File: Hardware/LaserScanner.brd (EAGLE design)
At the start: 160 x 100 mm, 35 parts, among them J1 USB, Q1 MBT3904DW1T1, U1 ESP-WROOM-32, U2 3.3V, U3 CH340C

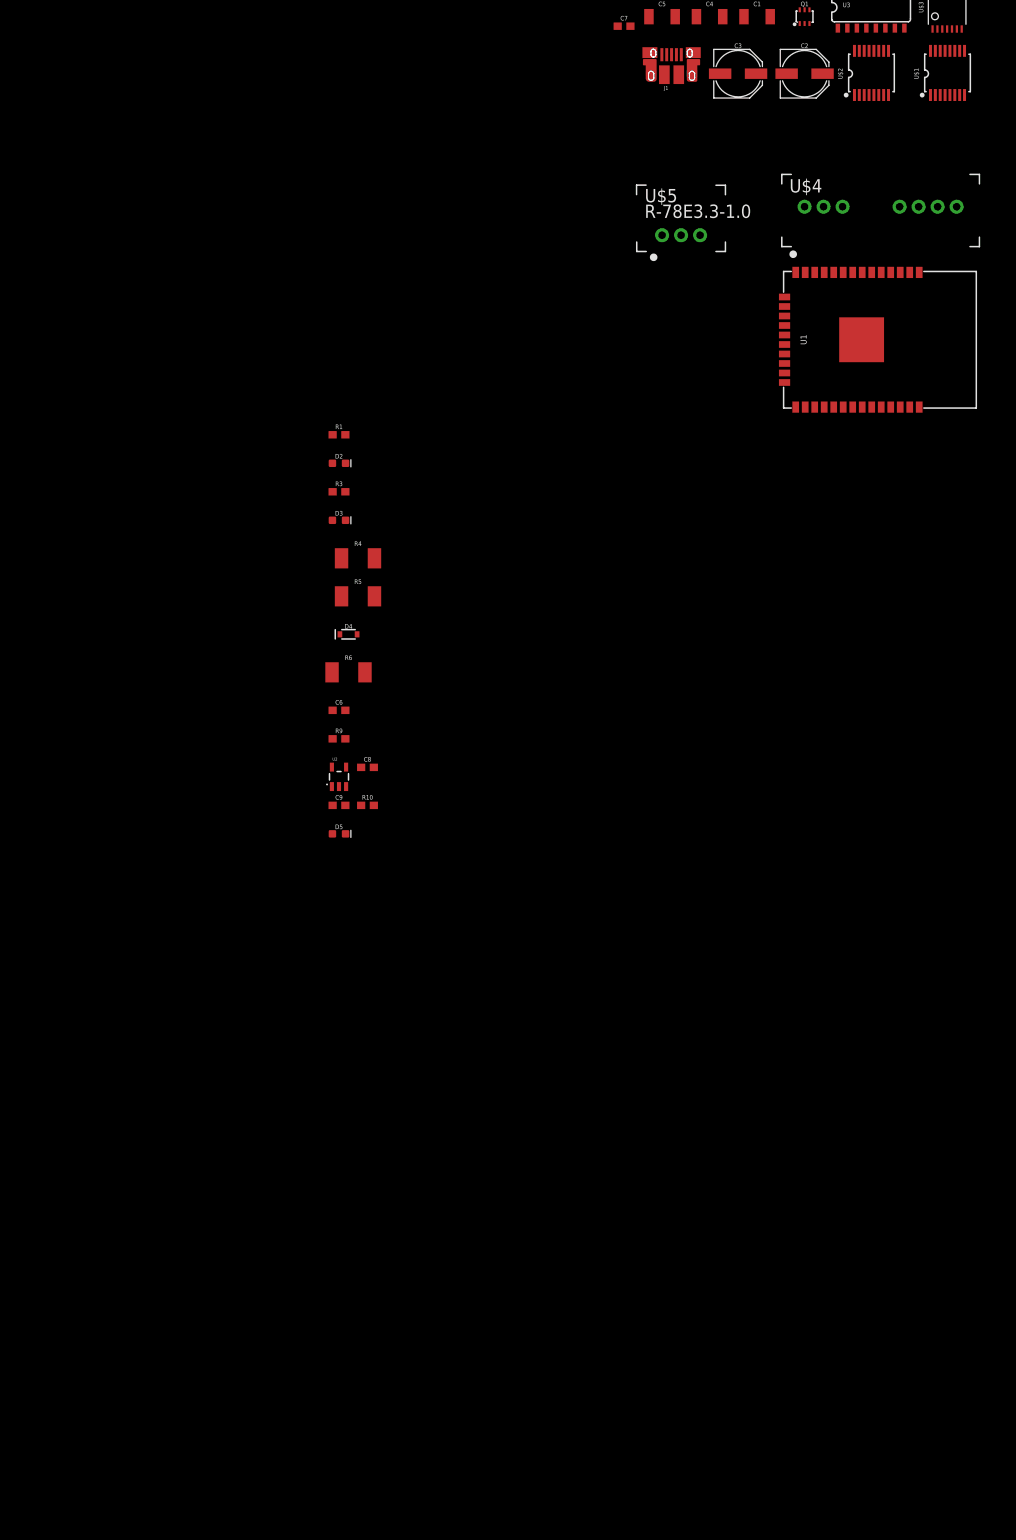
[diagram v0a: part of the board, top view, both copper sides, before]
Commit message: Added DAC circuits and power interlocks
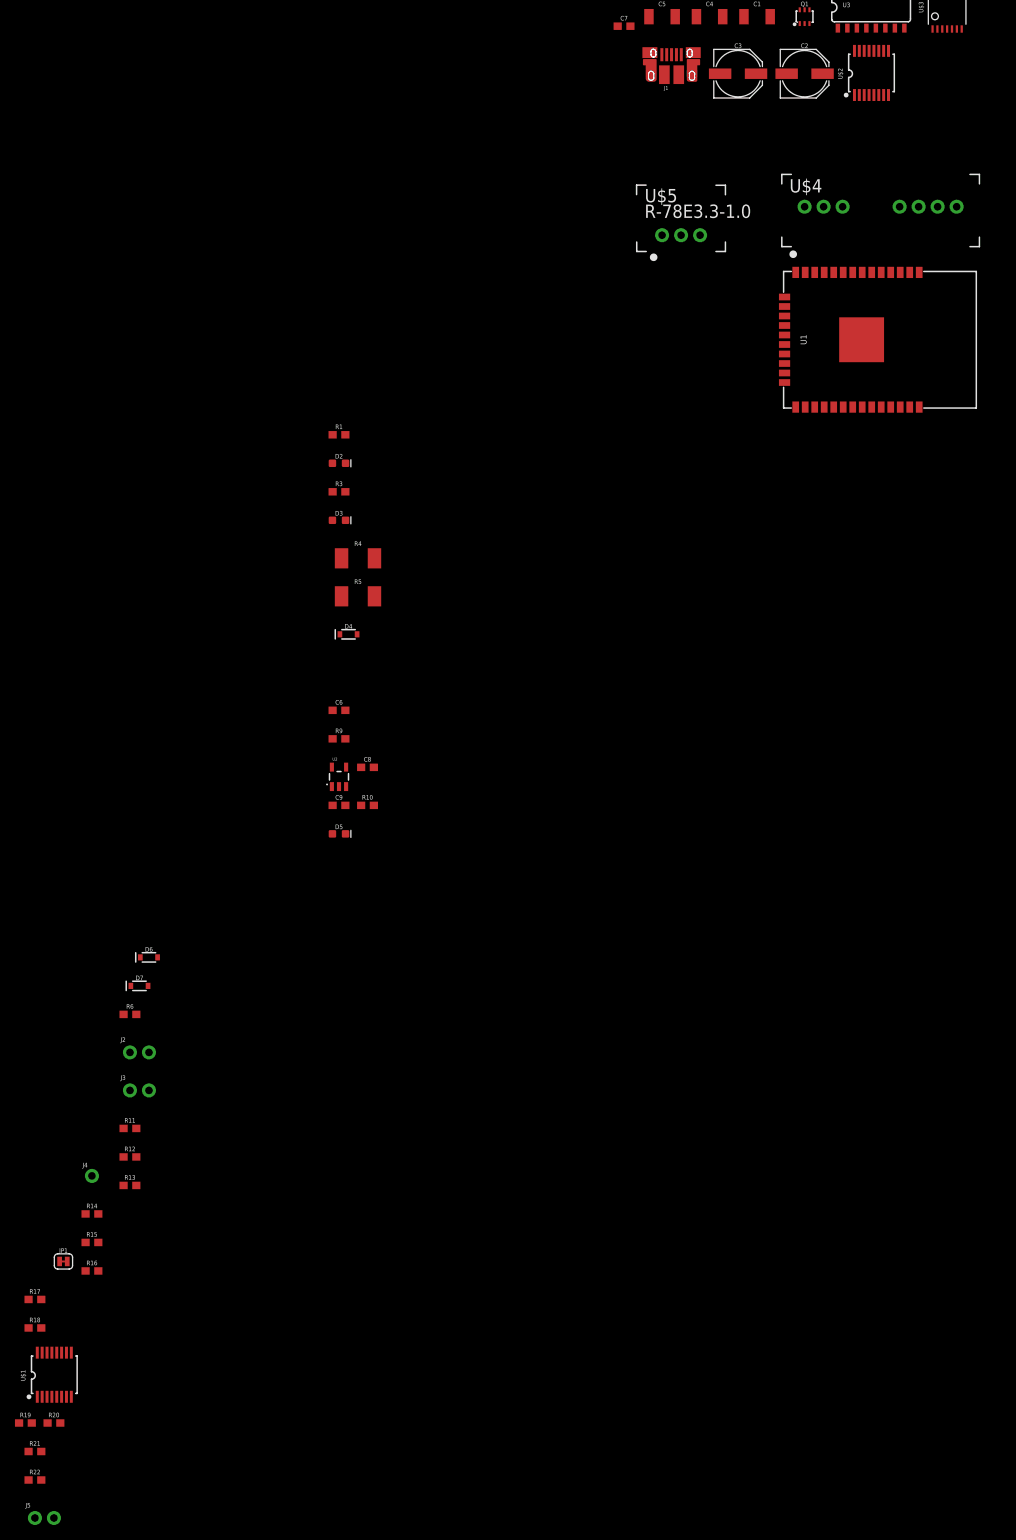
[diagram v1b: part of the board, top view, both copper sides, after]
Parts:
- added D6, D7: 3A/10V/280mV, SparkFun-DiscreteSemi:SOD-323
- added J2: SHTDWN, SparkFun-Connectors:1X02_NO_SILK
- added J3: KEYSWITCH, SparkFun-Connectors:1X02_NO_SILK
- added J4: (no value), SparkFun-Connectors:1X01_NO_SILK
- added J5: ESTOP, SparkFun-Connectors:1X02_NO_SILK
- added JP1: JUMPER-SMT_2_NC_TRACE_SILK, SparkFun-Jumpers:SMT-JUMPER_2_NC_TRACE_SILK
- added R11, R12, R13, R14, R15, R16, R17, R18, R19, R20, R21, R22: 10k, SparkFun-Resistors:0603
- R6: value 510 -> 3.3k; device SparkFun-Resistors:2010 -> SparkFun-Resistors:0603
- moved U$1 211.0 mm to (-137.2, -128.3)
- moved R6 54.3 mm to (-127.0, -80.0)
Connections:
- new net AGND: JP1.1, U$1.4, U$2.4
- new net AUX_OUT: J4.1, R14.2, U$3.10
- new net GX_!CS: R17.1, U$2.12
- new net GX_!LDAC: R18.1, U$2.15
- new net GX_!RST: U$2.11
- new net GX_OUT: U$2.1
- new net GY_!CS: R19.1, U$1.12
- new net GY_!LDAC: R20.1, U$1.15
- new net GY_!RST: U$1.11
- new net GY_OUT: U$1.1
- new net G_MOSI: U$1.14, U$2.14
- new net G_SCLK: U$1.13, U$2.13
- new net LASER_B: R13.2, U$3.5
- new net LASER_G: R12.2, U$3.11
- new net LASER_R: R11.2, U$3.4
- new net L_!CLR: R15.1, U$3.9
- new net L_!LDAC: R21.1, U$3.1
- new net L_!SYNC: R22.1, U$3.2
- new net L_MOSI: U$3.13
- new net L_SCLK: U$3.14
- new net N$7: C4.1, D6.A, U$5.3
- new net N$9: J3.2, J5.1
- new net VCC: J2.1, J5.2
- new net VCC_SWITCHED: C5.1, J3.1, U$4.2
- new net VREFH: U$1.5, U$1.6, U$2.5, U$2.6
- new net VREFL: U$1.7, U$1.8, U$2.7, U$2.8
- net -12V: now also U$1.3, U$2.3
- net 12V: now also U$1.2, U$2.2
- net 3.3V: now also R15.2, R17.2, R18.2, R19.2, R20.2, R21.2, R22.2, U$1.10, U$1.9, U$2.10, U$2.9
- net 5V: now also C8.1, D6.C, D7.C, U$3.3, U$3.7, U2.1, U2.3; no longer C4.1, U$5.3
- net GND: now also JP1.2, R11.1, R12.1, R13.1, R14.1, R16.1, U$1.16, U$2.16, U$3.12, U$3.6
- net N$2: now also R16.2, U$3.8; no longer C5.1, U$4.2
- net N$4: now also R6.2; no longer R6.1
- net SHTDWN: now also J2.2, R6.1; no longer R6.2
- net V_USB: now also D7.A; no longer C8.1, U2.1, U2.3

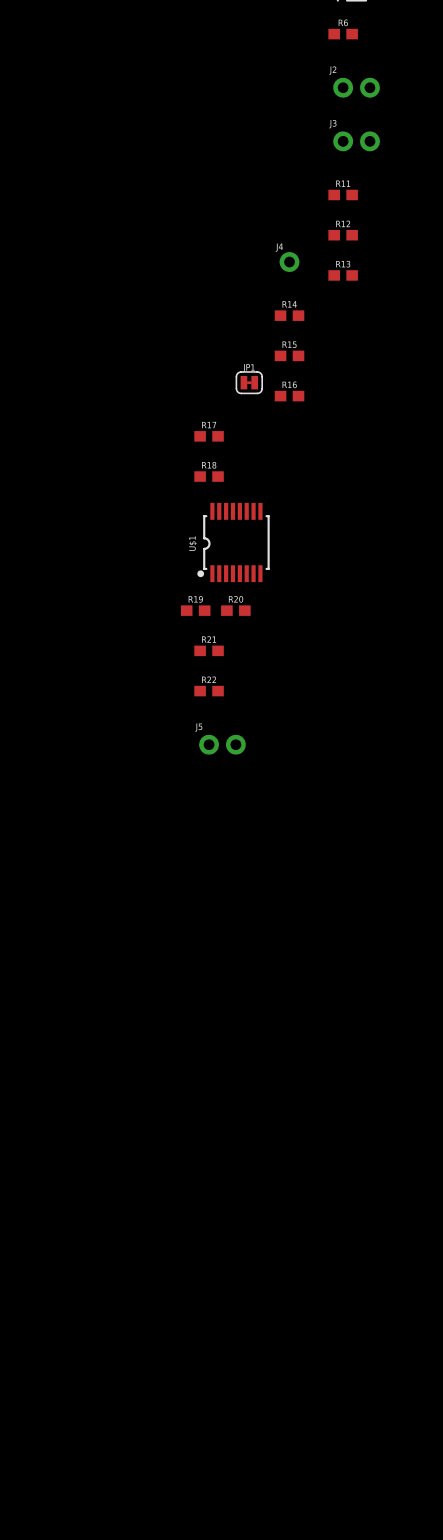
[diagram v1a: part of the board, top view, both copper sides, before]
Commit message: Add KILL signal and VREF delay
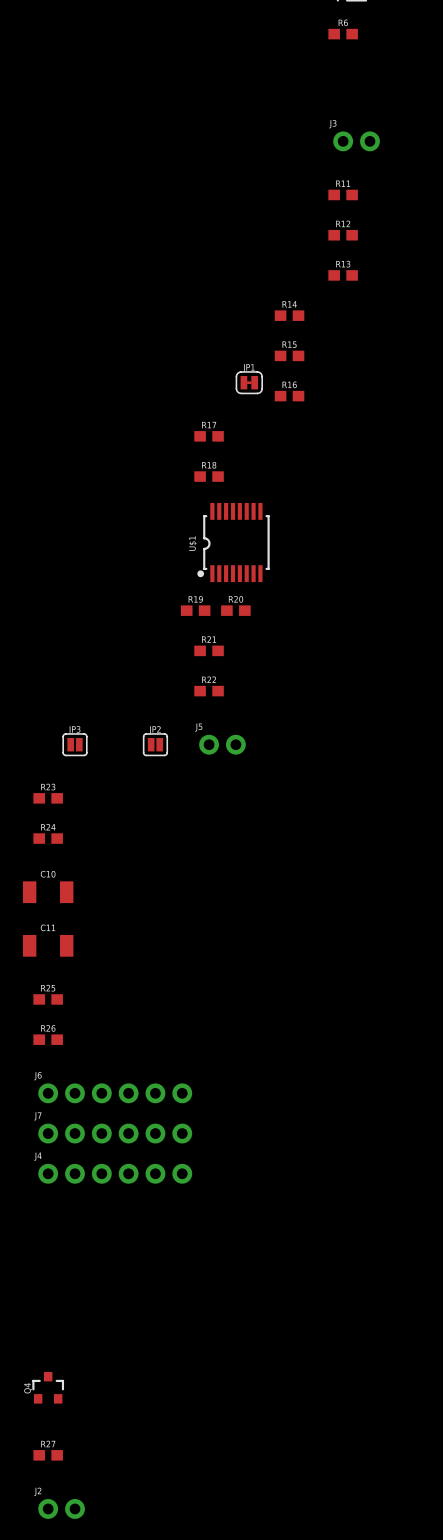
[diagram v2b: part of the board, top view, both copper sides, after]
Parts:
- added C10, C11: 10uF, SparkFun-Capacitors:1210
- added J6, J7: (no value), SparkFun-Connectors:1X06_NO_SILK
- added JP2, JP3: JUMPER-SMT_2_NO_SILK, SparkFun-Jumpers:SMT-JUMPER_2_NO_SILK
- added Q4: 2.5A/30V/105mΩ, SparkFun-DiscreteSemi:SOT23-3
- added R23, R24, R25, R26, R27: 10k, SparkFun-Resistors:0603
- J2: value SHTDWN -> !KILL!
- J4: device SparkFun-Connectors:1X01_NO_SILK -> SparkFun-Connectors:1X06_NO_SILK
- moved J2 137.5 mm to (-154.9, -219.7)
- moved J4 89.3 mm to (-154.9, -188.0)
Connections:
- removed net MISO: U1.14
- removed net MOSI: U1.16
- removed net SCLK: U1.13
- new net !KILL: J2.2, Q4.1, R27.2
- new net N$11: U1.29
- new net N$22: U1.8
- new net N$23: U1.9
- new net N$24: U1.6
- new net N$25: U1.7
- new net N$8: U1.26
- net -12V: now also JP3.1, R23.1
- net 12V: now also JP2.1, R24.1
- net 3.3V: now also R25.2, R26.2
- net AGND: now also C10.2, C11.2, J7.1, J7.2, J7.3, J7.4, J7.5, J7.6
- net AUX_OUT: now also J6.6; no longer J4.1
- net GND: now also J4.1, J4.2, J4.3, J4.4, J4.5, J4.6, R27.1
- net GX_!CS: now also U1.33
- net GX_!LDAC: now also U1.31
- net GX_!RST: now also R25.1, U1.36
- net GX_OUT: now also J6.1
- net GY_!CS: now also U1.27
- net GY_!LDAC: now also U1.23
- net GY_!RST: now also R26.1, U1.28
- net GY_OUT: now also J6.2
- net G_MOSI: now also U1.16
- net G_SCLK: now also U1.13
- net LASER_B: now also J6.5
- net LASER_G: now also J6.4
- net LASER_R: now also J6.3
- net L_!CLR: now also U1.10
- net L_!LDAC: now also U1.12
- net L_!SYNC: now also U1.11
- net L_MOSI: now also U1.37
- net L_SCLK: now also U1.30
- net SHTDWN: now also Q4.3; no longer J2.2
- net VCC: now also Q4.2
- net VREFH: now also C10.1, JP2.2, R24.2
- net VREFL: now also C11.1, JP3.2, R23.2

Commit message: RC calculations
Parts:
- removed JP1: JUMPER-SMT_2_NC_TRACE_SILK, SparkFun-Jumpers:SMT-JUMPER_2_NC_TRACE_SILK
- added C12, C13, C14, C15, C16, C17: 1.0uF, SparkFun-Capacitors:0603
- added C18, C19, C20, C21, C22: 10uF, SparkFun-Capacitors:EIA3216
- added D8: GREEN, SparkFun-LED:LED-0603
- added D9: Yellow, SparkFun-LED:LED-0603
- added J8: Power Input, SparkFun-Connectors:1X02_NO_SILK
- added R28, R29: 1k, SparkFun-Resistors:0603
- added R30, R31: 10k, SparkFun-Resistors:0603
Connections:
- new net N$13: D8.A, R28.1
- new net N$14: D9.A, R29.1
- new net N$15: R24.2, R30.1
- new net N$16: R23.2, R31.1
- net -12V: now also C19.+, C21.+
- net 12V: now also C18.+, C20.+
- net 3.3V: now also C17.1, R28.2, R29.2
- net 5V: now also C16.1, C22.+
- net AGND: now also C12.2, C13.2, C14.2, C15.2; no longer C10.2, C11.2, J7.1, J7.2, J7.3, J7.4, J7.5, J7.6, JP1.1, U$1.4, U$2.4
- net GND: now also C10.2, C11.2, C16.2, C17.2, C18.-, C19.-, C20.-, C21.-, C22.-, J7.1, J7.2, J7.3, J7.4, J7.5, J7.6, J8.2, U$1.4, U$2.4; no longer JP1.2
- net RXI: now also D9.C
- net TXO: now also D8.C
- net VCC: now also J8.1
- net VREFH: now also C13.1, C15.1, R30.2; no longer R24.2
- net VREFL: now also C12.1, C14.1, R31.2; no longer R23.2

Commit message: Push to work from laptop
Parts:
- removed C11, C5: 10uF, SparkFun-Capacitors:1210
- added R32: 10k, SparkFun-Resistors:0603
- added S1: RESET, SparkFun-Switches:TACTILE_SWITCH_SMD_4.6X2.8MM
- added S2: 0, SparkFun-Switches:TACTILE_SWITCH_SMD_4.6X2.8MM
- C1, C10, C4: device SparkFun-Capacitors:1210 -> SparkFun-Capacitors:EIA3216
- U$5: value R-78E3.3-1.0 -> 12to5
- moved R31 498.7 mm to (151.1, 96.5)
- moved R30 493.7 mm to (151.1, 94.0)
- moved C21 491.1 mm to (154.9, 96.5)
- moved C20 485.2 mm to (154.9, 94.0)
- moved C22 461.1 mm to (107.3, 89.7)
- moved C19 431.6 mm to (117.3, 60.6), turned to 180 degrees
- moved J8 431.1 mm to (153.7, 40.6)
- moved C18 429.8 mm to (117.3, 63.2), turned to 180 degrees
- moved C16 425.2 mm to (111.3, 91.6)
- moved C15 414.7 mm to (122.6, 72.0), turned to 90 degrees
- moved C14 410.9 mm to (121.0, 72.0), turned to 90 degrees
- moved J2 410.4 mm to (153.7, 50.8)
- moved R27 409.7 mm to (154.9, 53.3)
- moved C13 397.6 mm to (122.0, 56.6), turned to 90 degrees
- moved C12 393.8 mm to (120.5, 56.6), turned to 90 degrees
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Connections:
- removed net AGND: C12.2, C13.2, C14.2, C15.2
- net -12V: no longer C21.+
- net 0: now also R32.1, S2.3, S2.4
- net 12V: now also C1.+; no longer C1.1, C20.+
- net 3.3V: now also R32.2
- net GND: now also C1.-, C10.-, C12.2, C13.2, C14.2, C15.2, C21.+, C4.-, S1.1, S1.2, S2.1, S2.2; no longer C1.2, C10.2, C11.2, C21.-, C4.2, C5.2
- net N$7: now also C4.+; no longer C4.1
- net RESET: now also S1.3, S1.4
- net VCC_SWITCHED: now also C10.+; no longer C5.1
- net VREFH: now also C20.+; no longer C10.1
- net VREFL: now also C21.-; no longer C11.1

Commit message: Made a significant push on routing the board
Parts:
- removed R32: 10k, SparkFun-Resistors:0603
- removed S1: RESET, SparkFun-Switches:TACTILE_SWITCH_SMD_4.6X2.8MM
- removed S2: 0, SparkFun-Switches:TACTILE_SWITCH_SMD_4.6X2.8MM
- added R33: 10k, SparkFun-Resistors:0603
- added S3: USW2, SparkFun-Switches:TACTILE_SWITCH_SMD_5.2MM
- added S4: USW3, SparkFun-Switches:TACTILE_SWITCH_SMD_5.2MM
- moved J8 152.0 mm to (2.54, 24.1), turned to 90 degrees
- moved J7 115.6 mm to (63.5, 73.7)
- moved J6 114.6 mm to (61.0, 73.7)
- moved R31 112.7 mm to (41.9, 68.6), turned to 90 degrees
- moved R30 111.3 mm to (41.9, 72.4), turned to 90 degrees
- moved R23 110.3 mm to (40.6, 68.6), turned to 270 degrees
- moved R24 108.8 mm to (40.6, 72.4), turned to 270 degrees
- moved JP3 106.6 mm to (41.9, 68.6), flipped to the bottom
- moved C21 106.3 mm to (52.1, 69.8), turned to 180 degrees
- moved C20 105.1 mm to (52.1, 72.4)
- moved JP2 105.1 mm to (41.9, 72.4), flipped to the bottom
- moved R12 81.2 mm to (47.0, 96.5), turned to 270 degrees
- moved R13 77.9 mm to (48.3, 83.8), turned to 90 degrees
- moved R11 77.7 mm to (47.0, 83.8), turned to 90 degrees
- moved R14 76.6 mm to (48.3, 96.5), turned to 270 degrees
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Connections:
- net -12V: now also C19.-; no longer C19.+
- net 0: now also R33.1, S3.1, S3.2; no longer R32.1, S2.3, S2.4
- net 3.3V: now also R33.2; no longer R32.2
- net GND: now also C19.+, S3.3, S3.4, S4.3, S4.4; no longer C19.-, S1.1, S1.2, S2.1, S2.2
- net LASER_B: now also J6.3; no longer J6.5
- net LASER_G: now also J6.5; no longer J6.4
- net LASER_R: now also J6.4; no longer J6.3
- net RESET: now also S4.1, S4.2; no longer S1.3, S1.4
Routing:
- net 12V: track 0.00 -> 58.9 mm, vias 0 -> 1
- net GND: track 0.00 -> 48.3 mm
- net VREFH: track 0.00 -> 45.6 mm, vias 0 -> 5
- net -12V: track 0.00 -> 44.5 mm, vias 0 -> 3
- net VREFL: track 0.00 -> 39.7 mm, vias 0 -> 4
- net G_SCLK: track 0.00 -> 33.2 mm, vias 0 -> 2
- net G_MOSI: track 0.00 -> 29.7 mm, vias 0 -> 2
- net 3.3V: track 0.00 -> 22.5 mm
- net LASER_R: track 0.00 -> 22.3 mm
- net LASER_B: track 0.00 -> 21.9 mm
- net GY_!LDAC: track 0.00 -> 21.8 mm, vias 0 -> 1
- net LASER_G: track 0.00 -> 21.6 mm
- net GX_OUT: track 0.00 -> 20.2 mm
- net AUX_OUT: track 0.00 -> 19.7 mm
- net GX_!CS: track 0.00 -> 18.2 mm
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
